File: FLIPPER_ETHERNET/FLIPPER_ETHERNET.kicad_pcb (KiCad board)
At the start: 2 copper layers, 67 x 25 mm, 38 parts, among them J1 RJ45_Hanrun_HR911105A_Horizon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, J2 Conn_01x08_Socket, J3 Conn_01x10_Socket, U1 ENC28J60x-ML, Y1 25MHz

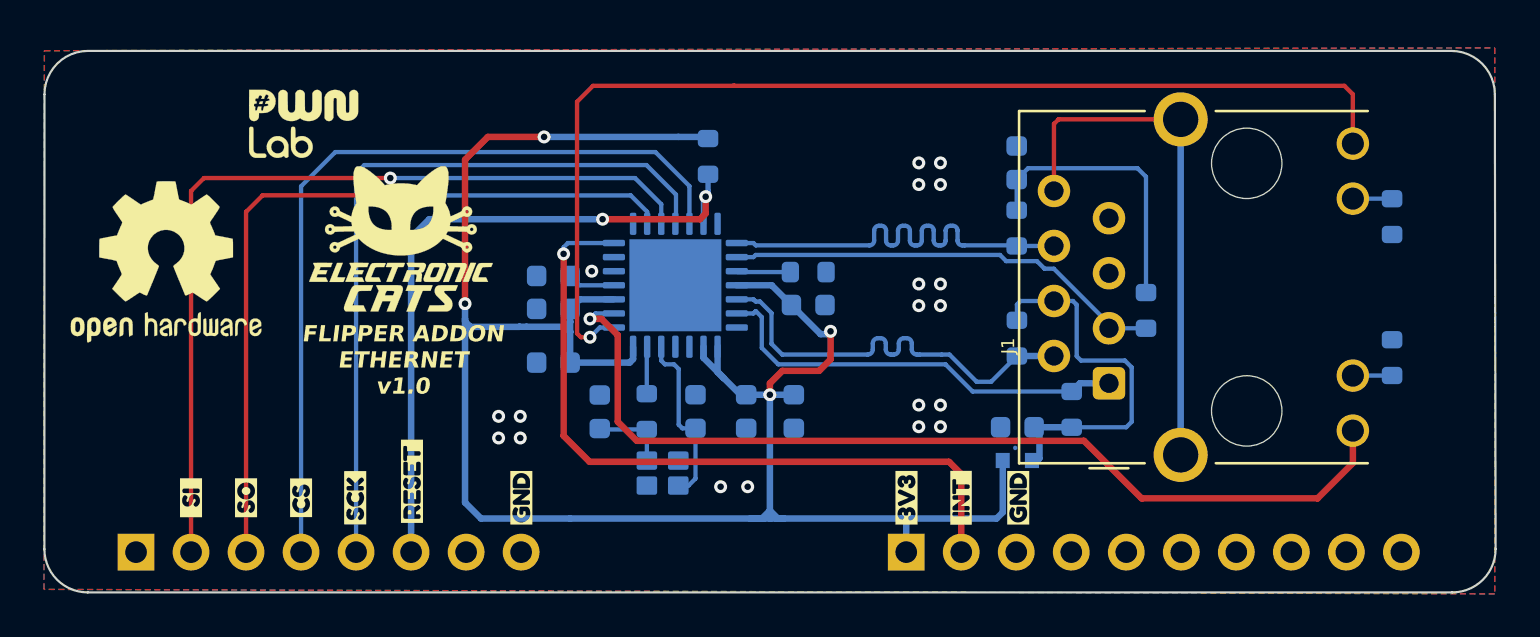
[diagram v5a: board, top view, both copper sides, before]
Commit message: refactor(hw): move components
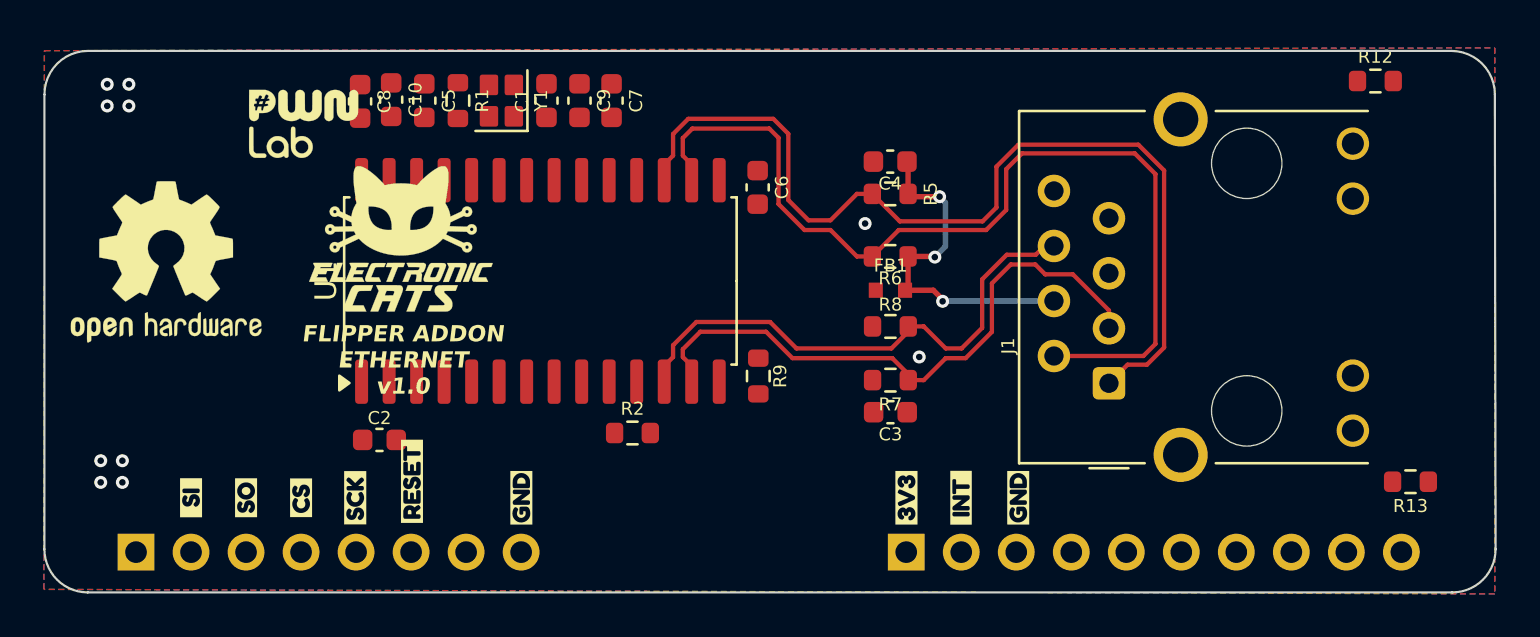
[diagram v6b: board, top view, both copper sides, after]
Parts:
- C1, C10, C2, C3, C4, C5, C6, C7, C8, C9, FB1, R1, R12, R13, R2, R5, R6, R7, R8, R9, Y1: moved to F.Cu
- U1: value ENC28J60x-ML -> ENC28J60x-SO; footprint Package_DFN_QFN:QFN-28-1EP_6x6mm_P0.65mm_EP4.25x4.25mm -> Package_SO:SOIC-28W_7.5x17.9mm_P1.27mm; moved to F.Cu
- moved Y1 18.7 mm to (137.1, 47.4), turned to 90 degrees
- moved R1 16.8 mm to (135.1, 47.4), turned to -90 degrees
- moved C7 16.6 mm to (142.2, 47.4), turned to 90 degrees
- moved C5 16.5 mm to (133.6, 47.4), turned to -90 degrees
- moved C9 16.3 mm to (140.7, 47.4), turned to -90 degrees
- moved C1 15.9 mm to (139.2, 47.4)
- moved C10 14.3 mm to (132.0, 47.4), turned to -90 degrees
- moved C4 13.6 mm to (155.1, 50.2)
- moved R2 13.2 mm to (143.2, 62.8), turned to 180 degrees
- moved C8 13.1 mm to (130.6, 47.5), turned to -90 degrees
- moved R5 13.0 mm to (155.1, 51.7), turned to 0 degrees
- moved C3 12.9 mm to (155.1, 61.8), turned to 0 degrees
- moved R7 12.2 mm to (155.1, 60.3), turned to 180 degrees
- moved C2 11.0 mm to (131.5, 63.1), turned to 0 degrees
- moved FB1 9.80 mm to (155.1, 56.2)
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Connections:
- U1 pad 1: unconnected-(U1-~{WOL}-Pad1) -> Net-(U1-VCAP)
- U1 pad 10: Net-(U1-RBIAS) -> /RESET
- U1 pad 11: +3.3V -> GND
- U1 pad 12: /TD- -> /RD-
- U1 pad 13: /TD+ -> /RD+
- U1 pad 14: GND -> Net-(U1-RBIAS)
- U1 pad 16: +3.3V -> /TD-
- U1 pad 17: GND -> /TD+
- U1 pad 19: /OSC1 -> +3.3V
- U1 pad 2: /SO -> GND
- U1 pad 20: /OSC2 -> +3.3V
- U1 pad 21: +3.3V -> GND
- U1 pad 22: /LEDB -> GND
- U1 pad 23: /LEDA -> /OSC1
- U1 pad 24: +3.3V -> /OSC2
- U1 pad 25: Net-(U1-VCAP) -> +3.3V
- U1 pad 26: GND -> /LEDB
- U1 pad 27: unconnected-(U1-CLKOUT-Pad27) -> /LEDA
- U1 pad 28: /INT -> +3.3V
- U1 pad 3: /SI -> unconnected-(U1-CLKOUT-Pad3)
- U1 pad 4: /SCK -> /INT
- U1 pad 5: /CS -> unconnected-(U1-~{WOL}-Pad5)
- U1 pad 6: /RESET -> /SO
- U1 pad 7: GND -> /SI
- U1 pad 8: /RD- -> /SCK
- U1 pad 9: /RD+ -> /CS
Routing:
- net +3.3V: track 96.6 -> 0.00 mm, vias 4 -> 0
- net /LEDB: track 51.3 -> 0.00 mm, vias 1 -> 0
- net /LEDA: track 44.4 -> 0.00 mm, vias 1 -> 0
- net /SI: track 40.0 -> 0.00 mm, vias 1 -> 0
- net /CS: track 37.9 -> 0.00 mm
- net /SO: track 35.4 -> 0.00 mm, vias 1 -> 0
- net /SCK: track 34.3 -> 0.00 mm
- net /INT: track 33.8 -> 0.00 mm, vias 1 -> 0
- net /RESET: track 31.7 -> 0.00 mm, vias 2 -> 0
- net /TD-: track 19.7 -> 44.6 mm
- net /TD+: track 19.7 -> 44.5 mm
- net Net-(J1-Pad8): track 24.5 -> 0.00 mm
- net Net-(C3-Pad1): track 13.1 -> 0.00 mm
- net /OSC1: track 8.27 -> 0.00 mm
- net /RD+: track 20.5 -> 28.0 mm
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
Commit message: feat(hw): add routes
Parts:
- removed the kibuzzard-6706FBB6 at (138.1, 65.8)
- removed kibuzzard-6706FD0C: G***, kibuzzard-6706FD0C
- removed kibuzzard-6706FEBD: G***, kibuzzard-6706FEBD
- removed kibuzzard-6706FECB: G***, kibuzzard-6706FECB
- removed kibuzzard-6706FEE4: G***, kibuzzard-6706FEE4
- removed kibuzzard-6835A348: G***, kibuzzard-6835A348
- added kibuzzard-684C6B2A: G***, kibuzzard-684C6B2A, F.Cu at (133.0, 65.8)
- added kibuzzard-684C6B35: G***, kibuzzard-684C6B35, F.Cu at (138.0, 66.0)
- added kibuzzard-684C6B3B: G***, kibuzzard-684C6B3B, F.Cu at (130.4, 65.8)
- added kibuzzard-684C6B3F: G***, kibuzzard-684C6B3F, F.Cu at (127.9, 66.1)
- added kibuzzard-684C6B44: G***, kibuzzard-684C6B44, F.Cu at (125.3, 66.2)
- added kibuzzard-684C6B5F: G***, kibuzzard-684C6B5F, F.Cu at (122.8, 66.2)
- REF**: moved to B.Cu
- moved G*** 25.1 mm to (147.5, 64.3)
- moved G*** 15.1 mm to (147.5, 52.7)
- moved C10 10.9 mm to (122.5, 52.6)
- moved C2 9.20 mm to (122.5, 61.3), turned to 90 degrees
- moved C6 8.63 mm to (140.8, 48.7), turned to 90 degrees
- moved FB1 7.65 mm to (153.5, 48.7), turned to 90 degrees
- moved R2 6.81 mm to (136.5, 64.0)
- moved G*** 6.53 mm to (139.0, 53.8)
- moved C1 6.52 mm to (132.8, 48.7)
- moved C7 6.52 mm to (135.8, 48.7)
- moved C9 6.52 mm to (134.3, 48.7)
- moved R1 6.52 mm to (128.7, 48.7)
- moved R9 6.52 mm to (142.6, 61.4)
- moved U1 6.52 mm to (132.5, 57.0)
- moved Y1 6.52 mm to (130.7, 48.7)
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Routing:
- net +3.3V: track 0.00 -> 97.8 mm, vias 0 -> 3
- net /LEDA: track 0.00 -> 78.2 mm, vias 0 -> 1
- net /LEDB: track 0.00 -> 62.0 mm, vias 0 -> 1
- net /INT: track 0.00 -> 36.3 mm, vias 0 -> 3
- net Net-(J1-Pad8): track 0.00 -> 23.9 mm
- net /SI: track 0.00 -> 19.7 mm, vias 0 -> 1
- net /CS: track 0.00 -> 16.4 mm, vias 0 -> 1
- net /RD-: track 24.6 -> 40.3 mm, vias 0 -> 1
- net /RD+: track 28.0 -> 40.5 mm, vias 0 -> 1
- net /SO: track 0.00 -> 11.1 mm
- net /RESET: track 0.00 -> 9.02 mm
- net Net-(C3-Pad1): track 0.00 -> 8.75 mm, vias 0 -> 2
- net Net-(J1-Pad10): track 0.00 -> 8.35 mm, vias 0 -> 1
- net /SCK: track 0.00 -> 8.24 mm
- net Net-(J1-Pad11): track 0.00 -> 7.03 mm, vias 0 -> 1
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
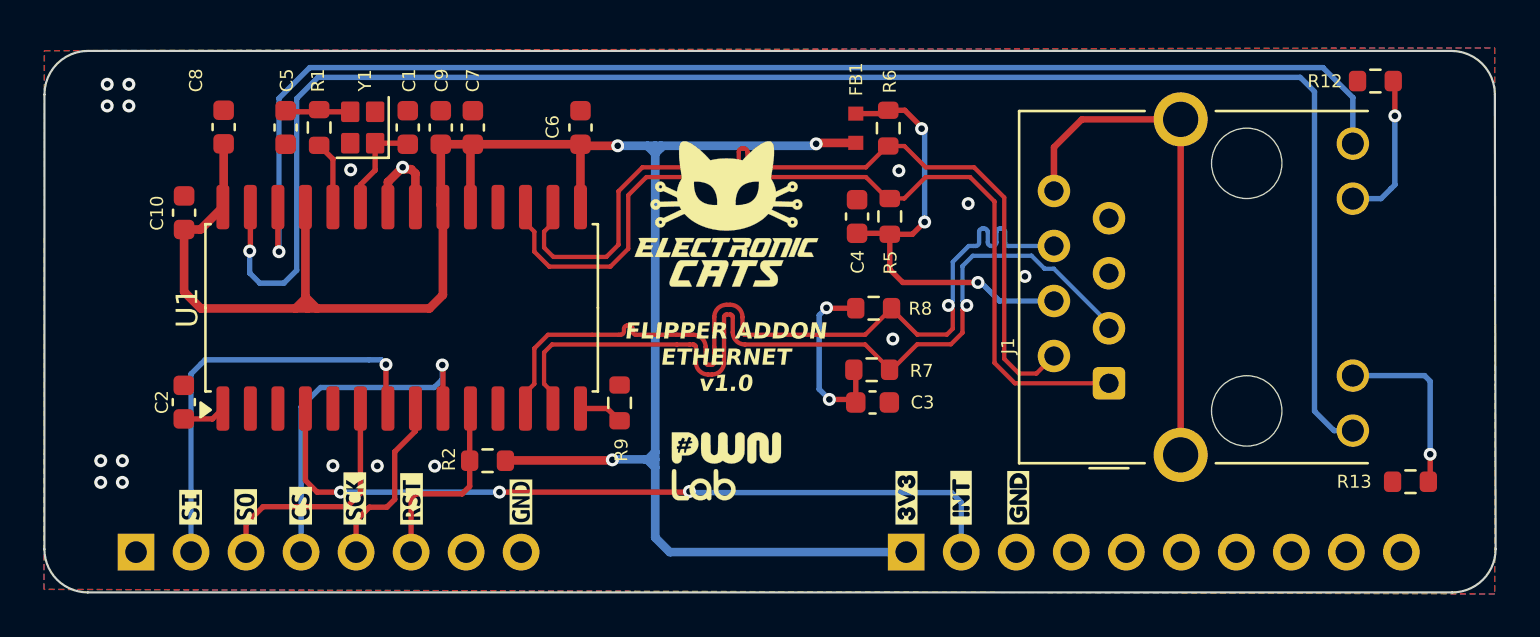
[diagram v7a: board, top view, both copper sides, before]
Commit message: fix(hw): modify the characteristics of the differential pair
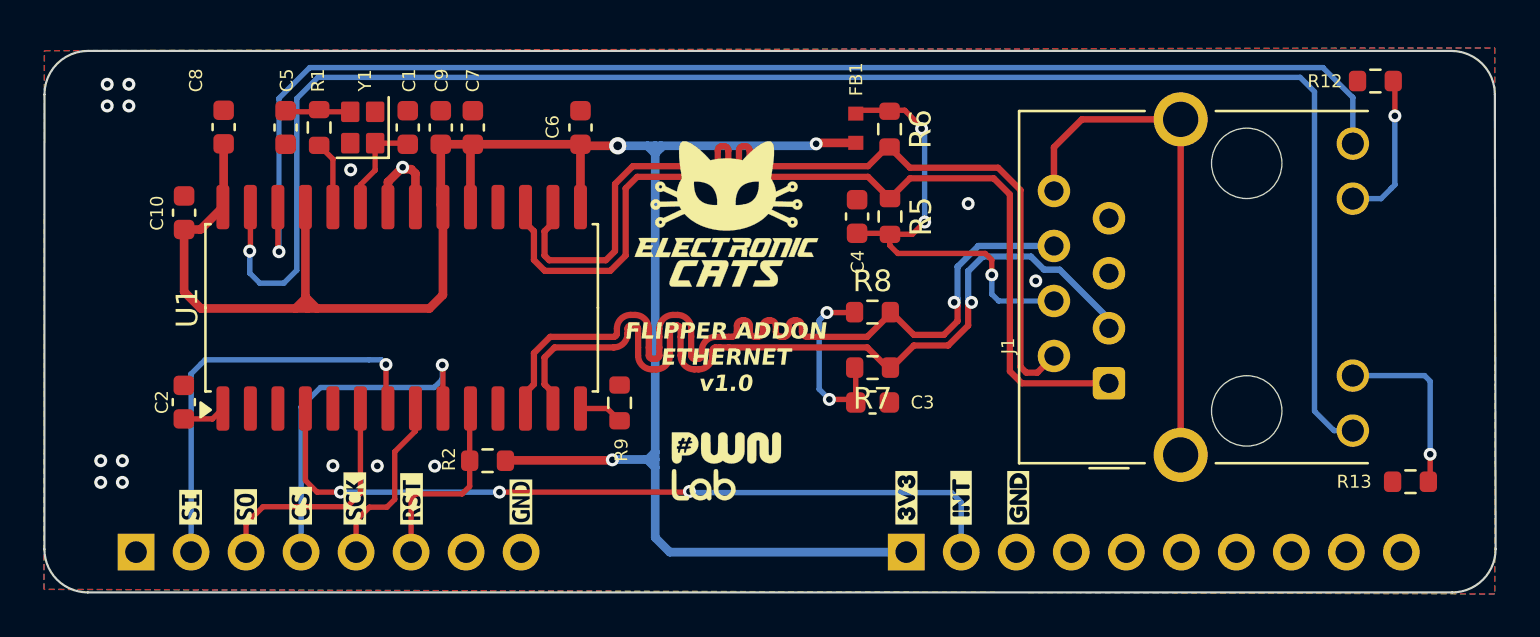
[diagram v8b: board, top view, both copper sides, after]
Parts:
- moved R8 0.19 mm to (154.3, 57.2)
- moved R7 0.11 mm to (154.3, 59.8)
- moved R6 0.08 mm to (155.1, 48.7)
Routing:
- net /TD+: track 41.3 -> 42.5 mm
- net /TD-: track 41.3 -> 42.4 mm
- net GND: vias 17 -> 15
